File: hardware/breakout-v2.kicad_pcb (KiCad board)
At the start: 2 copper layers, 40 x 25 mm, 22 parts, among them P1 Port A, P2 CONN_01X05, P3 CONN_01X02, P4 CONN_01X03, P5 Port B, Q1 2N7002, U1 AP7333, U2 74AHC244, U3 DRILL, U4 DRILL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

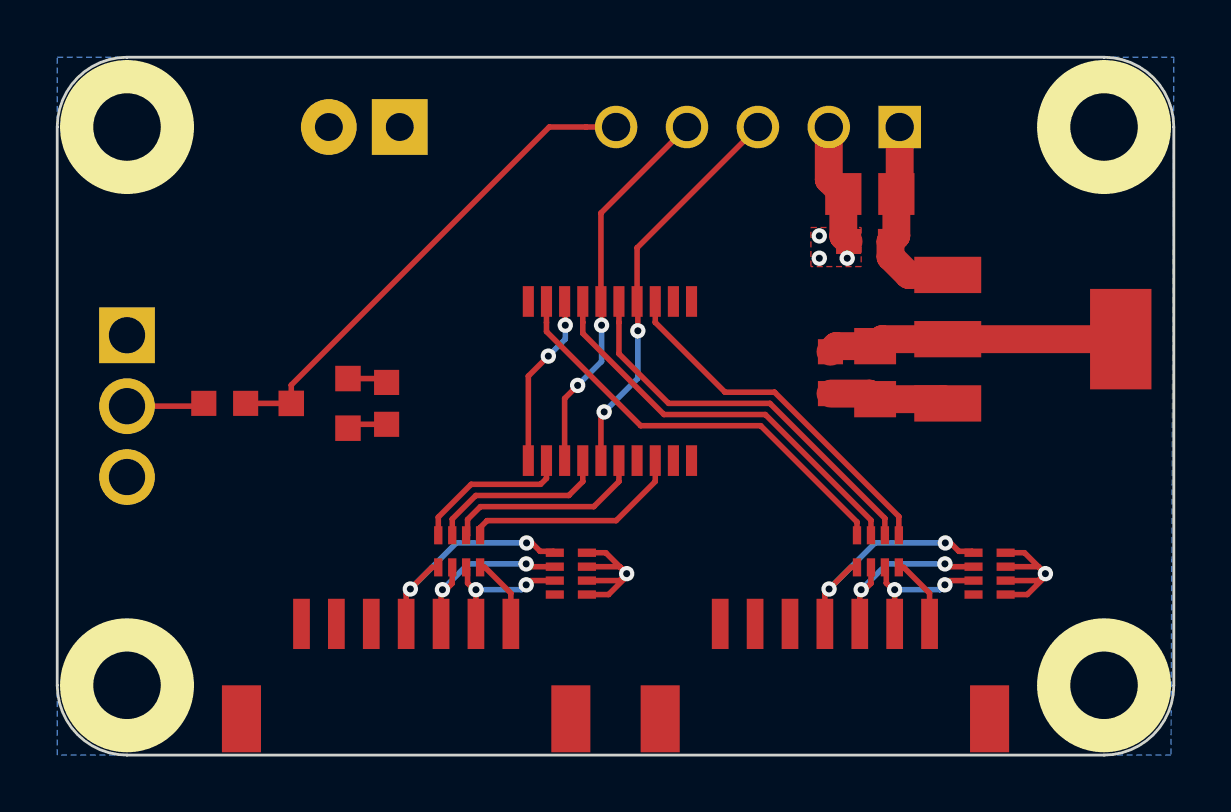
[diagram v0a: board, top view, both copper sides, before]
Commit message: edited silksreen
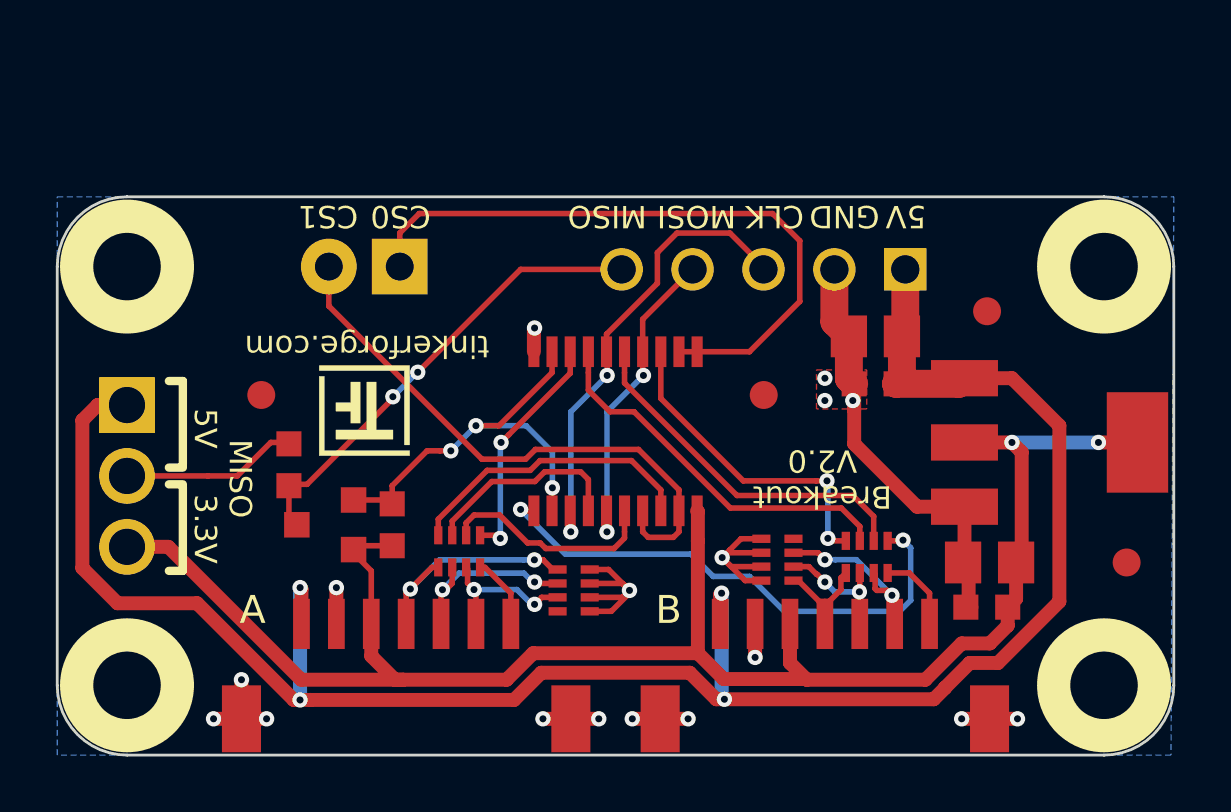
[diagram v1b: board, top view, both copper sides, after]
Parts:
- added Fiducial_Mark: VAL**, kicad-libraries:Fiducial_Mark, F.Cu at (132.0, 92.0)
- added Fiducial_Mark: VAL**, kicad-libraries:Fiducial_Mark, F.Cu at (145.0, 98.0)
- added Fiducial_Mark: VAL**, kicad-libraries:Fiducial_Mark, F.Cu at (140.0, 89.0)
- added Fiducial_Mark: VAL**, kicad-libraries:Fiducial_Mark, F.Cu at (114.0, 92.0)
- added G***: LOGO, kicad-libraries:Logo_31x31, F.Cu at (117.7, 92.5)
- added VAL: CE_5mm, kicad-libraries:CE_5mm, B.Cu at (130.6, 95.7)
- added VAL: WEEE_7mm, kicad-libraries:WEEE_7mm, B.Cu at (123.4, 95.5)
- moved C4 10.1 mm to (140.0, 99.6), turned to 180 degrees
- moved C3 7.94 mm to (140.1, 98.0), turned to 180 degrees
- moved CP2 7.62 mm to (132.5, 97.9), turned to 90 degrees
- moved C1 5.10 mm to (136.0, 89.9)
- moved C2 5.10 mm to (136.0, 91.6)
- moved P2 5.10 mm to (132.0, 87.5)
- moved P3 5.00 mm to (117.7, 87.4)
- moved U4 5.00 mm to (144.2, 87.4)
- moved U6 5.00 mm to (109.2, 87.4)
- moved Q1 4.35 mm to (116.3, 96.7)
- moved R2 4.35 mm to (118.7, 96.7)
- moved U1 3.75 mm to (142.3, 93.7)
- moved R1 3.18 mm to (115.0, 94.5), turned to 270 degrees
- moved P4 2.50 mm to (109.2, 94.9)
- moved U2 1.81 mm to (126.7, 93.3)
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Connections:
- U2 pad 11: CS1 -> Net-(RP2-Pad1)
- U2 pad 12: Net-(RP1-Pad4) -> Net-(Q1-PadS)
- U2 pad 17: Net-(Q1-PadS) -> CS1
- U2 pad 18: Net-(RP1-Pad1) -> Net-(RP1-Pad4)
- U2 pad 2: Net-(Q1-PadS) -> CS0
- U2 pad 3: Net-(RP2-Pad1) -> Net-(RP2-Pad4)
- U2 pad 8: CS0 -> Net-(RP1-Pad1)
- U2 pad 9: Net-(RP2-Pad4) -> Net-(Q1-PadS)
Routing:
- net +5V: track 7.11 -> 73.8 mm, vias 0 -> 4
- net +3.3VP: track 12.0 -> 62.6 mm, vias 0 -> 2
- net CS0: track 0.00 -> 23.5 mm
- net CS1: track 0.00 -> 20.7 mm
- net GND: track 21.9 -> 40.8 mm, vias 5 -> 17
- net Net-(Q1-PadS): track 7.70 -> 15.6 mm, vias 2 -> 3
- net Net-(RP2-Pad1): track 13.0 -> 19.0 mm, vias 0 -> 2
- net Net-(CP2-Pad1): track 8.64 -> 3.66 mm, vias 2 -> 0
- net Net-(RP1-Pad4): track 5.74 -> 10.6 mm
- net Net-(RP2-Pad4): track 15.5 -> 11.6 mm, vias 0 -> 2
- net Net-(P4-Pad2): track 2.79 -> 6.30 mm
- net CLK: track 14.3 -> 16.8 mm
- net MOSI: track 13.8 -> 11.5 mm
- net Net-(CP2-Pad2): track 6.64 -> 4.56 mm
- net Net-(RP2-Pad2): track 14.5 -> 12.9 mm
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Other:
- board size 40 x 25 mm -> 40 x 20 mm
- net class Default: clearance 0.2 -> 0.149
- rule trace_clearance: 0.2 -> 0.149
- board text added: "3.3V"
- board text added: "5V"
- board text added: "A"
- board text added: "B"
- board text added: "Breakout V2.0"
- board text added: "CLK"
- board text added: "CS0"
- board text added: "CS1"
- board text added: "GND"
- board text added: "MISO"
- board text added: "MOSI"
- board text added: "tinkerforge.com"

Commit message: changed design
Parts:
- removed Fiducial_Mark (x4): VAL**, kicad-libraries:Fiducial_Mark
- added C5: 100nF, kicad-libraries:C0603F, F.Cu at (130.1, 95.3)
- added R3: 10k, kicad-libraries:R0603F, F.Cu at (114.1, 88.2)
- added R4: 10k, kicad-libraries:R0603F, F.Cu at (121.2, 88.3)
- added R5: 100, kicad-libraries:R0603F, F.Cu at (119.3, 92.2)
- added R6: 100, kicad-libraries:R0603F, F.Cu at (119.3, 90.9)
- added RP3: 100k, kicad-libraries:4X0402, F.Cu at (118.9, 94.4)
- G***: moved to B.Cu
- P2: footprint kicad-libraries:pin_array_5x1 -> kicad-libraries:pin_array_1x5-P2mm_D1mm
- P3: footprint kicad-libraries:PIN_ARRAY_2X1 -> kicad-libraries:pin_array_1x2-P2mm_D1mm
- P4: footprint kicad-libraries:PIN_ARRAY_3X1 -> kicad-libraries:pin_array_1x3-P2mm_D1mm
- U1: value AP7333 -> LD1117
- moved G*** 25.6 mm to (143.2, 94.9), turned to 90 degrees
- moved Q1 5.33 mm to (114.7, 91.5)
- moved R2 5.33 mm to (117.1, 91.5)
- moved R1 4.57 mm to (112.3, 90.8), turned to 90 degrees
- moved VAL 3.10 mm to (120.3, 95.4)
- moved VAL 1.83 mm to (132.4, 95.4)
- moved U2 0.61 mm to (126.1, 93.2)
- moved U1 0.11 mm to (142.4, 93.7)
- moved P3 0.10 mm to (117.7, 87.5)
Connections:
- net CS0 renamed CS_A
- net CS1 renamed CS_B
- U1 pad 1: +5V -> GND
- U1 pad 3: GND -> +5V
- U2 pad 12: Net-(Q1-PadS) -> Net-(R5-Pad1)
- U2 pad 9: Net-(Q1-PadS) -> Net-(R6-Pad1)
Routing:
- net +3.3VP: track 62.6 -> 83.2 mm, vias 2 -> 0
- net Net-(Q1-PadS): track 15.6 -> 4.26 mm, vias 3 -> 0
- net Net-(RP2-Pad3): track 13.6 -> 23.0 mm, vias 0 -> 2
- net Net-(RP2-Pad4): track 11.6 -> 20.5 mm, vias 2 -> 0
- net Net-(R5-Pad1): track 0.00 -> 6.79 mm, vias 0 -> 2
- net +5V: track 73.8 -> 68.5 mm, vias 4 -> 6
- net MISO: track 17.0 -> 21.8 mm, vias 2 -> 1
- net Net-(R6-Pad1): track 0.00 -> 4.61 mm
- net Net-(RP2-Pad1): track 19.0 -> 15.2 mm
- net Net-(RP1-Pad3): track 7.35 -> 9.20 mm, vias 0 -> 2
- net CS_A: track 23.5 -> 24.7 mm
- net MOSI: track 11.5 -> 10.4 mm
- net Net-(RP2-Pad2): track 12.9 -> 13.8 mm, vias 0 -> 2
- net CLK: track 16.8 -> 17.5 mm
- net Net-(RP1-Pad1): track 8.49 -> 7.76 mm
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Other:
- board text added: "CS"
- board text added: "CS A"
- board text added: "CS B"
- board text removed: "CS0"
- board text removed: "CS1"

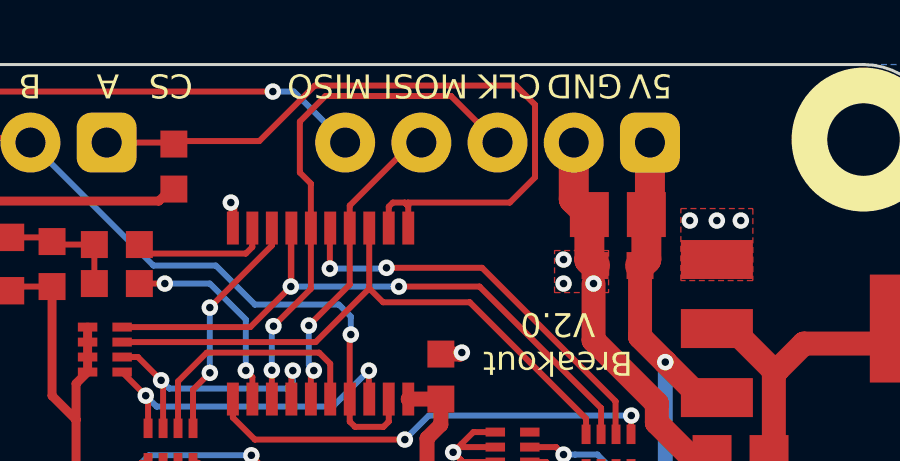
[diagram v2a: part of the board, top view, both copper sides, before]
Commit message: switched MISO and MOSI pin
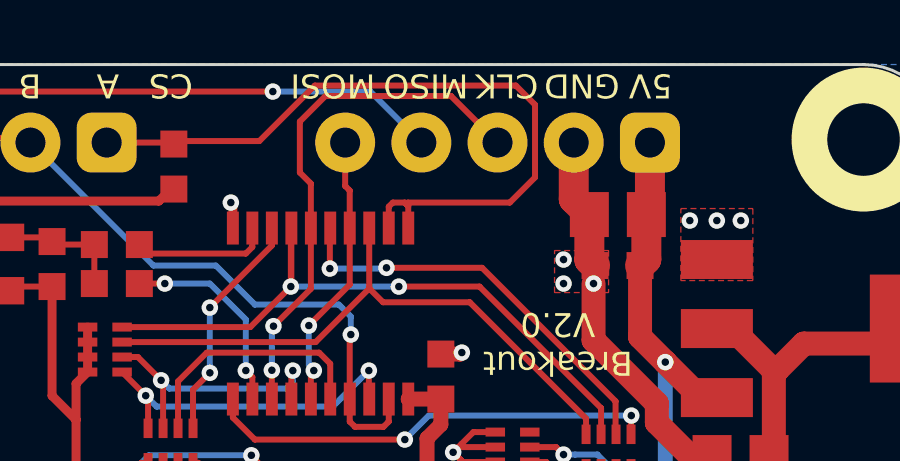
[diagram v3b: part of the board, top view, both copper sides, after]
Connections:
- P2 pad 4: MOSI -> MISO
- P2 pad 5: MISO -> MOSI
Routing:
- net MISO: track 21.8 -> 24.4 mm
- net MOSI: track 10.4 -> 9.30 mm
